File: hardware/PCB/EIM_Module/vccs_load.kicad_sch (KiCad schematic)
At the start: 43 parts, among them J2 CURRENT_PUMP_2, J3 VOLTAGE_MEASUREMENT_1, J4 VOLTAGE_MEASUREMENT_2, J8 CURRENT_PUMP_1, U4 AD8130ARZ, U5 AD8066ARZ-R7, U6 AD8130ARZ, U7 AD8066ARZ-R7, U8 AD8130ARZ

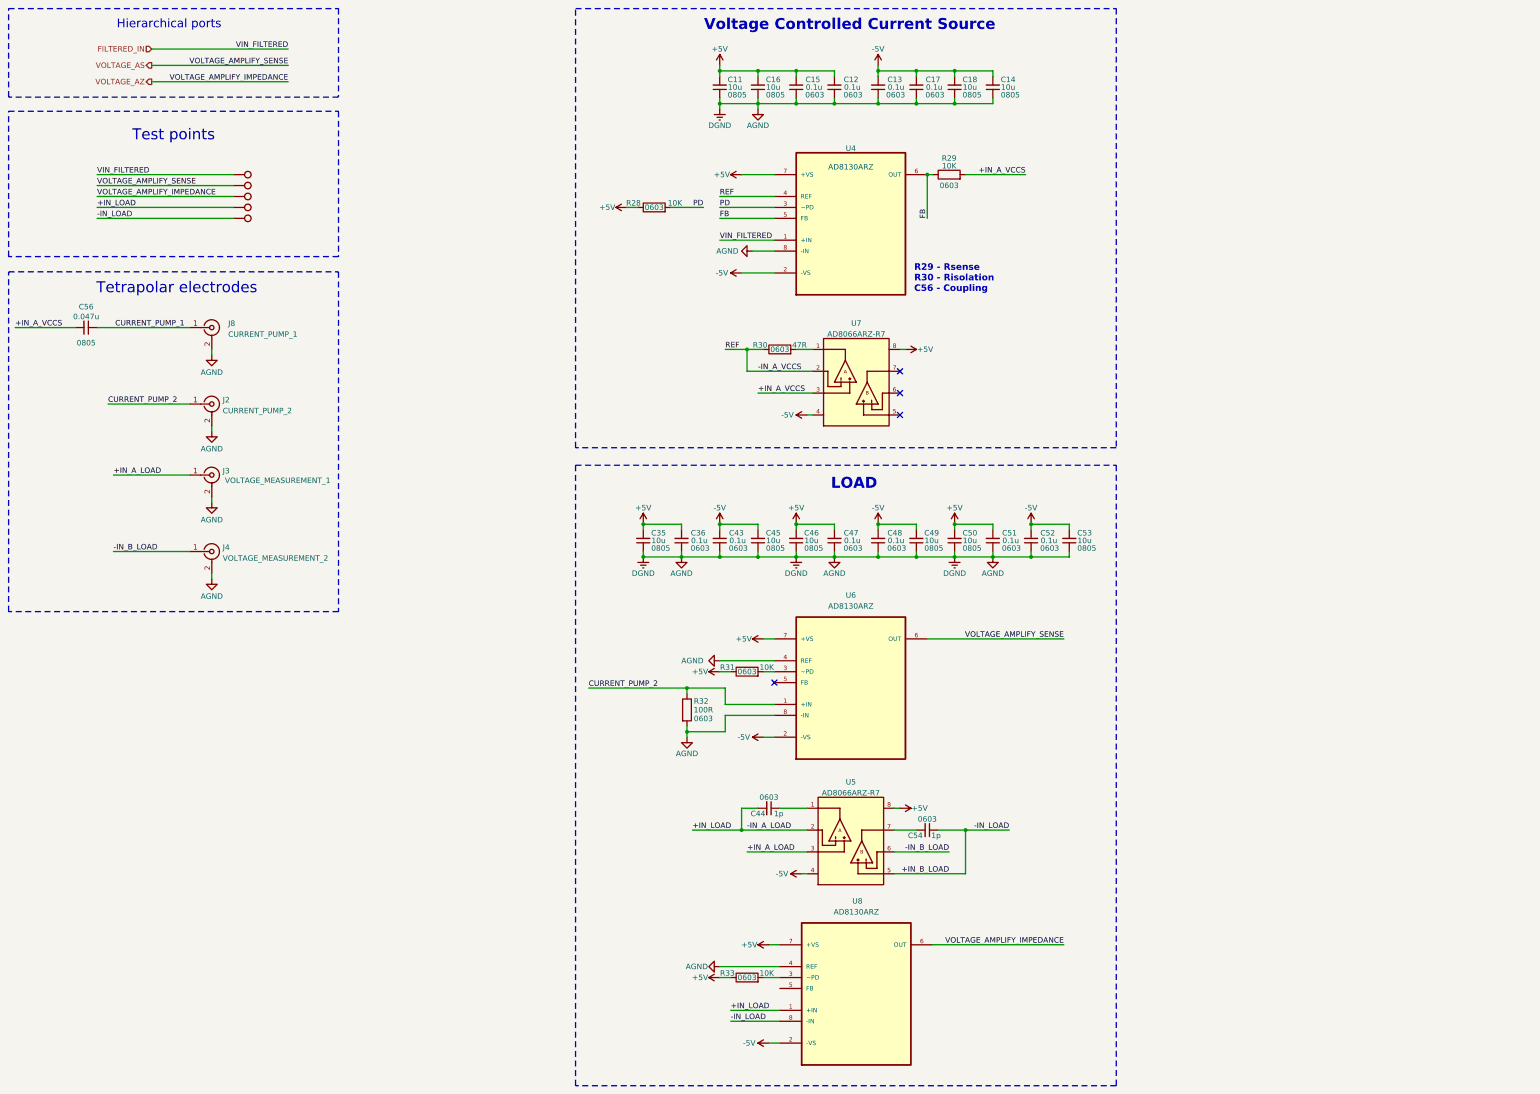
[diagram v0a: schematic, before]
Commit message: MAMS-33 Updated simulation final and update schematic and PCB
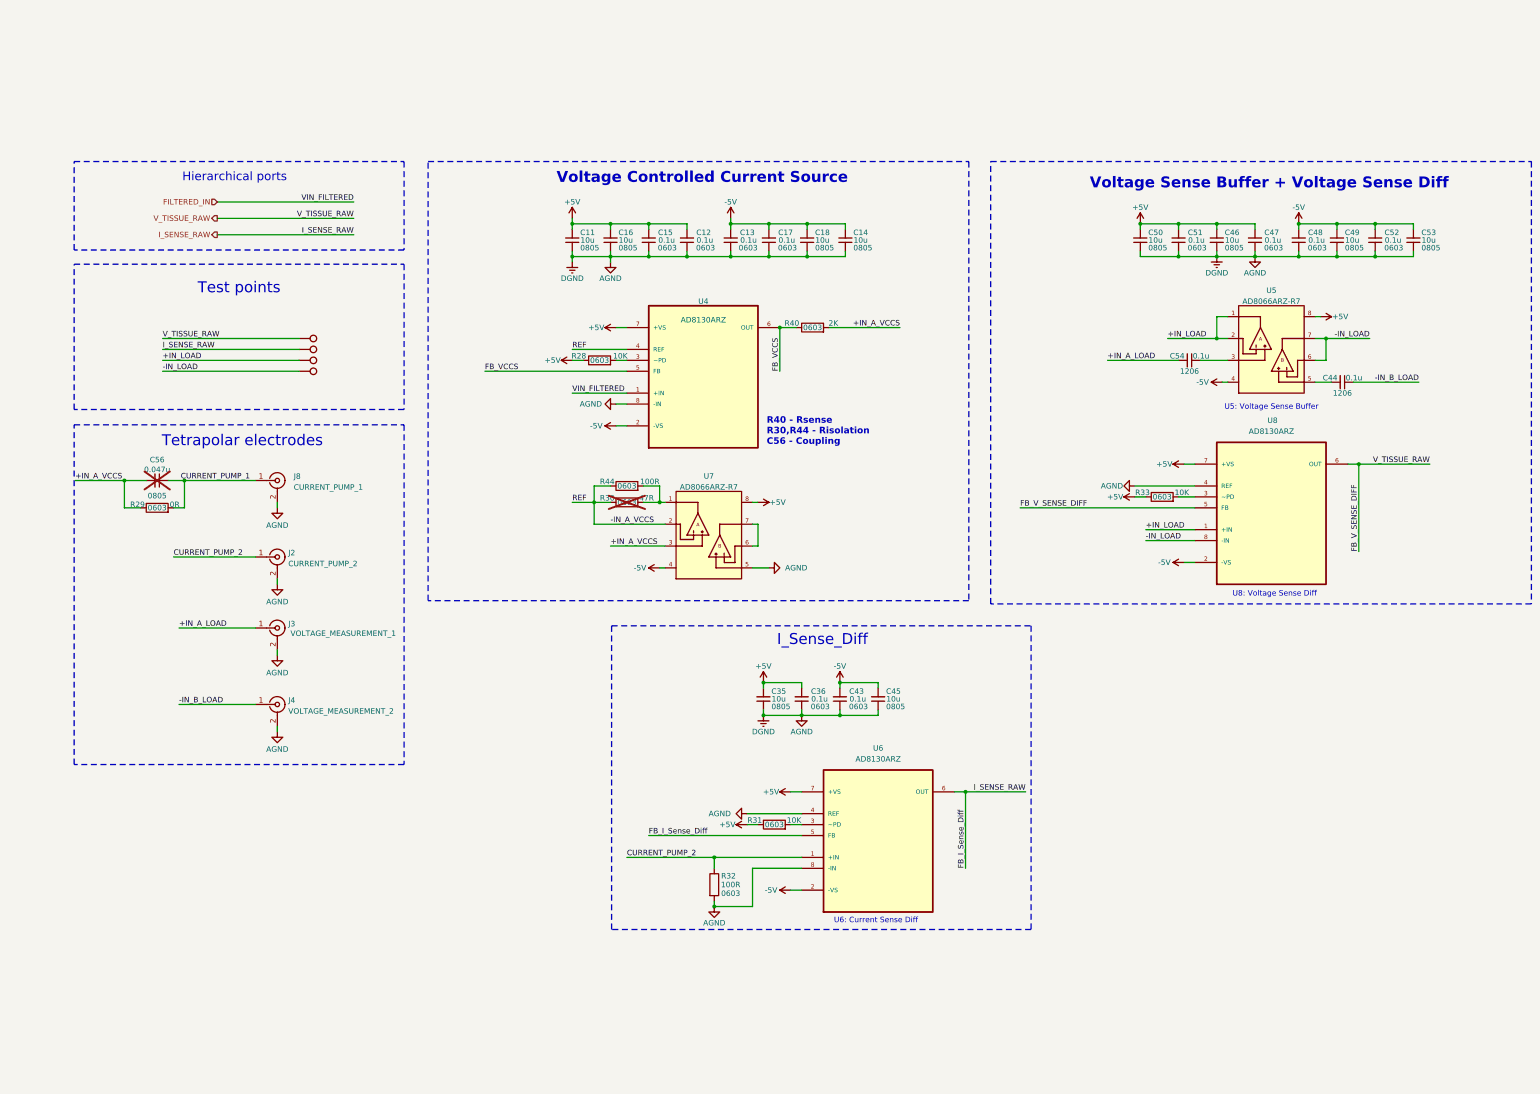
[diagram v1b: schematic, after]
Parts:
- removed TP16: VOUT_FILTERED, TestPoint:TestPoint_Pad_D1.0mm, symbol Connector:TestPoint
- added R40: 2K, Resistor_SMD:R_0603_1608Metric, symbol Device:R
- added R44: 100R, Resistor_SMD:R_0603_1608Metric, symbol Device:R
- C44, C54: value 1p -> 0.1u; footprint Capacitor_SMD:C_0603_1608Metric -> Capacitor_SMD:C_1206_3216Metric; Size 0603 -> 1206
- C56, R30: now not fitted
- J2, J3, J4, J8: footprint (none) -> Connector_Coaxial:SMA_Molex_73251-2200_Horizontal
- R29: value 10K -> 0R
- U5, U7: footprint AD8066ARZ-R7:SOIC127P600X175-8N -> AD8066ARZ:SOIC127P600X175-8N
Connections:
- net +IN_A_LOAD: now also C54.2; no longer U5.3
- net +IN_A_VCCS: now also R29.1, R40.2; no longer R29.2
- net +IN_LOAD: now also U5.1; no longer C44.2
- net -IN_A_VCCS: now also R44.1
- net -IN_B_LOAD: now also C44.1; no longer U5.6
- net AGND: now also U7.5
- net CURRENT_PUMP_1: now also R29.2
- net at R30.2, U7.1: now also R44.2
- net -IN_LOAD: now reaches U5.7
- net -IN_LOAD: now also TP20.1, U5.6, U8.8 (-IN); no longer C54.2
- net V_TISSUE_RAW: now reaches U8.5 (FB)
- net V_TISSUE_RAW: now also TP17.1, U8.6 (OUT)
- net at U7.6: now also U7.7
- net I_SENSE_RAW: now reaches U6.5 (FB)
- net I_SENSE_RAW: now also TP18.1, U6.6 (OUT)
- removed net +IN_B_LOAD: C54.1, TP20.1, U5.5, U8.8 (-IN)
- net FB renamed FB_VCCS
- net FB_VCCS: now also R40.1; no longer R29.1
- net PD: no longer names the net of R28.2, U4.3 (~PD)
- removed net VOLTAGE_AS: TP17.1, U6.6 (OUT)
- removed net VOLTAGE_AZ: TP18.1, U8.6 (OUT)
- new net: C54.1, U5.3
- new net: C44.2, U5.5
- no-connect marks 4 -> 0
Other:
- note added: "I_Sense_Diff"
- note added: "R40 - Rsense R30,R44 - Risolation C56 - Coupling"
- note added: "U5: Voltage Sense Buffer"
- note added: "U6: Current Sense Diff"
- note added: "U8: Voltage Sense Diff"
- note added: "Voltage Sense Buffer + Voltage Sense Diff"
- note removed: "LOAD"
- note removed: "R29 - Rsense R30 - Risolation C56 - Coupling"
- moved on the sheet: C11, C12, C13, C14, C15, C16, C17, C18, C35, C36, C43, C45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

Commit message: MAMS-38 updated PCB layout for EIM with version using connector
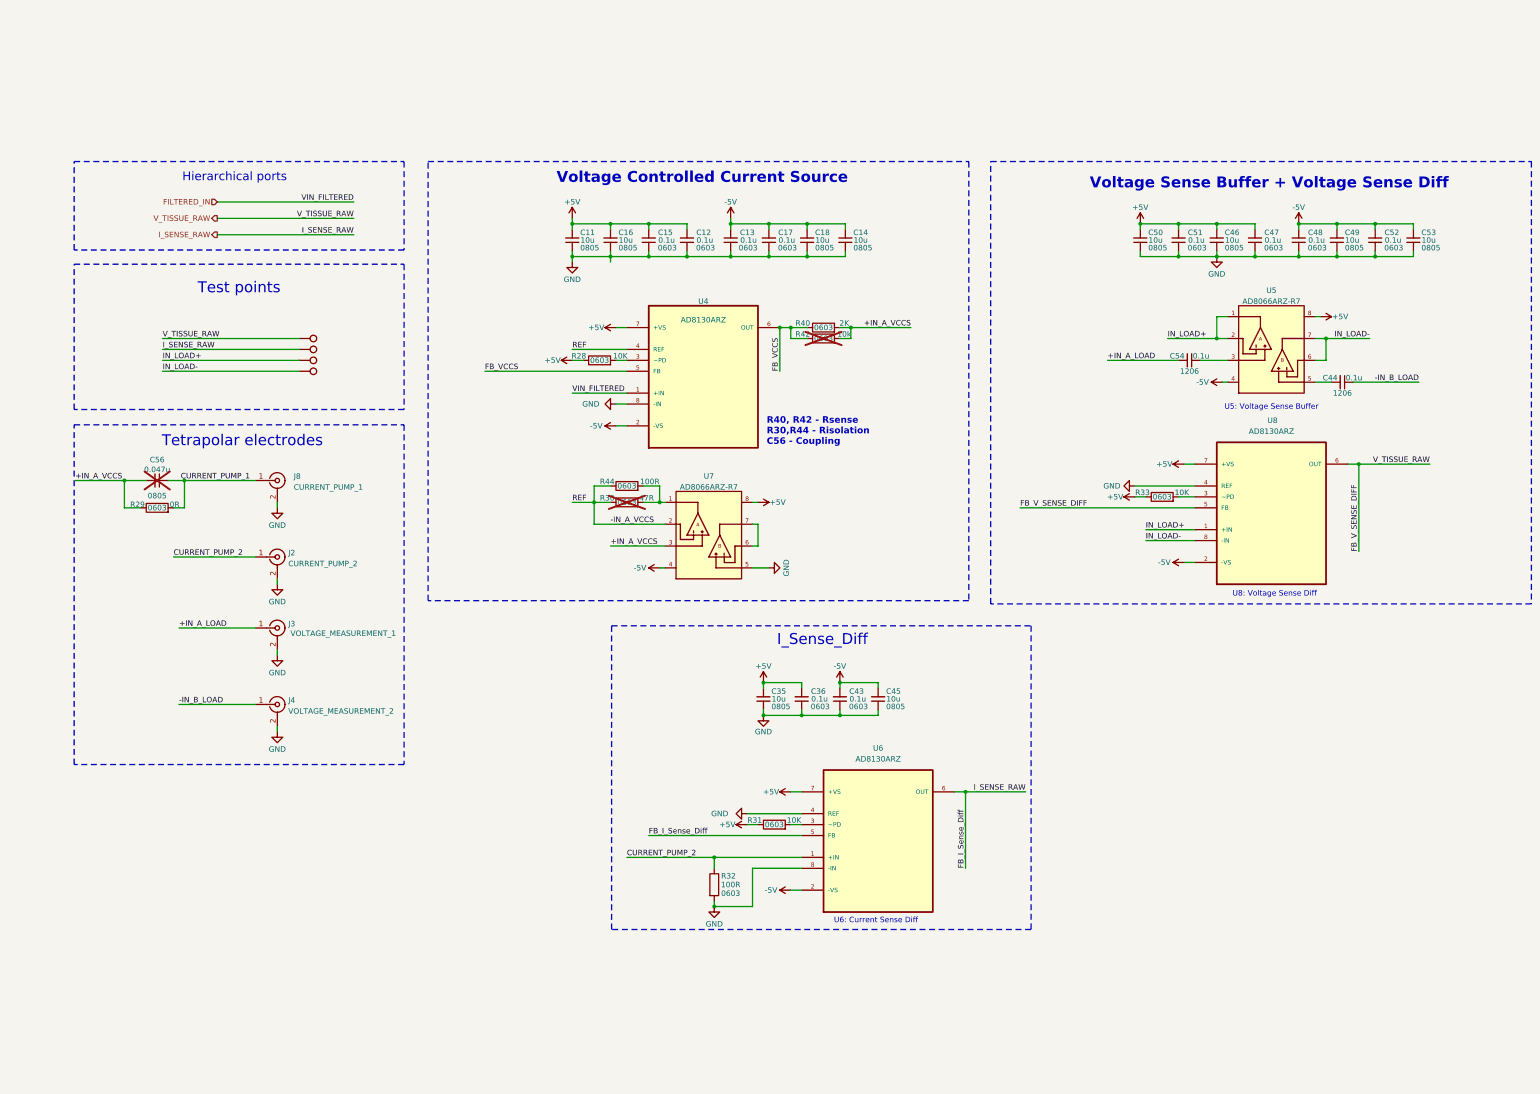
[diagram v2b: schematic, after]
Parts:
- added R42: 10k, Resistor_SMD:R_0603_1608Metric, symbol Device:R
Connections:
- net +IN_A_VCCS: now also R42.2
- net FB_VCCS: now also R42.1
- net +IN_LOAD renamed IN_LOAD+
- net -IN_LOAD renamed IN_LOAD-
- net AGND renamed GND
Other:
- note added: "R40, R42 - Rsense R30,R44 - Risolation C56 - Coupling"
- note removed: "R40 - Rsense R30,R44 - Risolation C56 - Coupling"
- moved on the sheet: R40

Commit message: MAMS-40 Updated PCB upto LPF
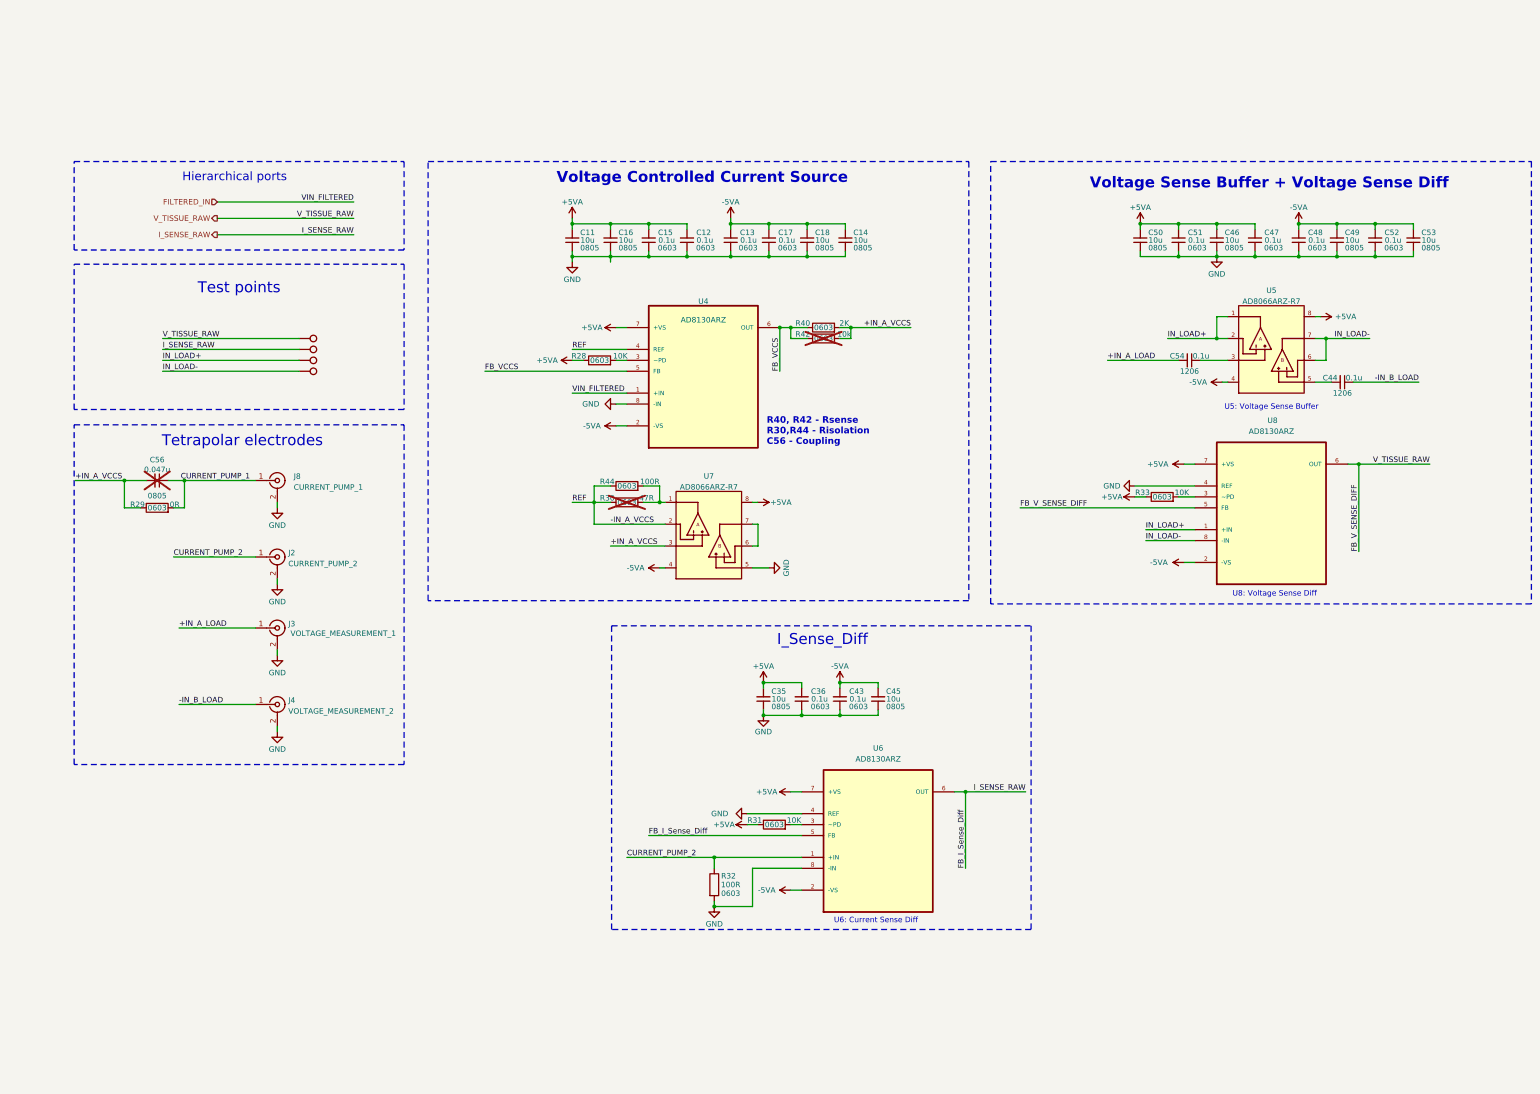
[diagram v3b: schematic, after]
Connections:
- net +5V renamed +5VA
- net -5V renamed -5VA
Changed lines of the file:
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@@
 			)
 		)
-		(property "Value" "+5V"
+		(property "Value" "+5VA"
 			(at 195.58 173.99 0)
 			(effects
@@
 			)
 		)
-		(property "Value" "+5V"
-			(at 288.798 127 90)
+		(property "Value" "+5VA"
+			(at 287.274 127 90)
 			(effects
 				(font
@@
 			)
 		)
-		(property "Value" "-5V"
-			(at 166.878 151.13 90)
+		(property "Value" "-5VA"
+			(at 165.862 151.13 90)
 			(effects
 				(font
@@
 			)
 		)
-		(property "Value" "+5V"
-			(at 329.692 92.71 90)
+		(property "Value" "+5VA"
+			(at 330.962 92.71 90)
 			(effects
 				(font
@@
 			)
 		)
-		(property "Value" "+5V"
-			(at 198.882 135.89 90)
+		(property "Value" "+5VA"
+			(at 199.644 135.89 90)
 			(effects
 				(font
@@
 			)
 		)
-		(property "Value" "+5V"
-			(at 187.198 210.82 90)
+		(property "Value" "+5VA"
+			(at 186.436 210.82 90)
 			(effects
 				(font
@@
 			)
 		)
-		(property "Value" "+5V"
-			(at 156.718 95.25 90)
+		(property "Value" "+5VA"
+			(at 155.702 95.25 90)
 			(effects
 				(font
@@
 			)
 		)
-		(property "Value" "+5V"
-			(at 146.558 102.87 90)
+		(property "Value" "+5VA"
+			(at 145.288 102.87 90)
 			(effects
 				(font
@@
 			)
 		)
-		(property "Value" "-5V"
-			(at 156.718 118.11 90)
+		(property "Value" "-5VA"
+			(at 155.702 118.11 90)
 			(effects
 				(font
@@
 			)
 		)
-		(property "Value" "+5V"
-			(at 197.358 203.2 90)
+		(property "Value" "+5VA"
+			(at 196.342 203.2 90)
 			(effects
 				(font
@@
 			)
 		)
-		(property "Value" "-5V"
-			(at 297.688 107.95 90)
+		(property "Value" "-5VA"
+			(at 296.672 107.95 90)
 			(effects
 				(font
@@
 			)
 		)
-		(property "Value" "-5V"
+		(property "Value" "-5VA"
 			(at 320.04 67.31 0)
 			(effects
@@
 			)
 		)
-		(property "Value" "-5V"
+		(property "Value" "-5VA"
 			(at 213.36 173.99 0)
 			(effects
@@
 			)
 		)
-		(property "Value" "+5V"
+		(property "Value" "+5VA"
 			(at 283.21 67.31 0)
 			(effects
@@
 			)
 		)
-		(property "Value" "+5V"
-			(at 277.368 134.62 90)
+		(property "Value" "+5VA"
+			(at 276.606 134.62 90)
 			(effects
 				(font
@@
 			)
 		)
-		(property "Value" "-5V"
+		(property "Value" "-5VA"
 			(at 187.96 66.04 0)
 			(effects
@@
 			)
 		)
-		(property "Value" "+5V"
+		(property "Value" "+5VA"
 			(at 151.13 66.04 0)
 			(effects
@@
 			)
 		)
-		(property "Value" "-5V"
-			(at 288.798 149.86 90)
+		(property "Value" "-5VA"
+			(at 287.528 149.86 90)
 			(effects
 				(font
@@
 			)
 		)
-		(property "Value" "-5V"
-			(at 197.358 226.06 90)
+		(property "Value" "-5VA"
+			(at 196.342 226.06 90)
 			(effects
 				(font
